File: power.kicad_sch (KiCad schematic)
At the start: 2 parts, among them J301 Conn_01x01_Socket, J302 Conn_01x01_Socket

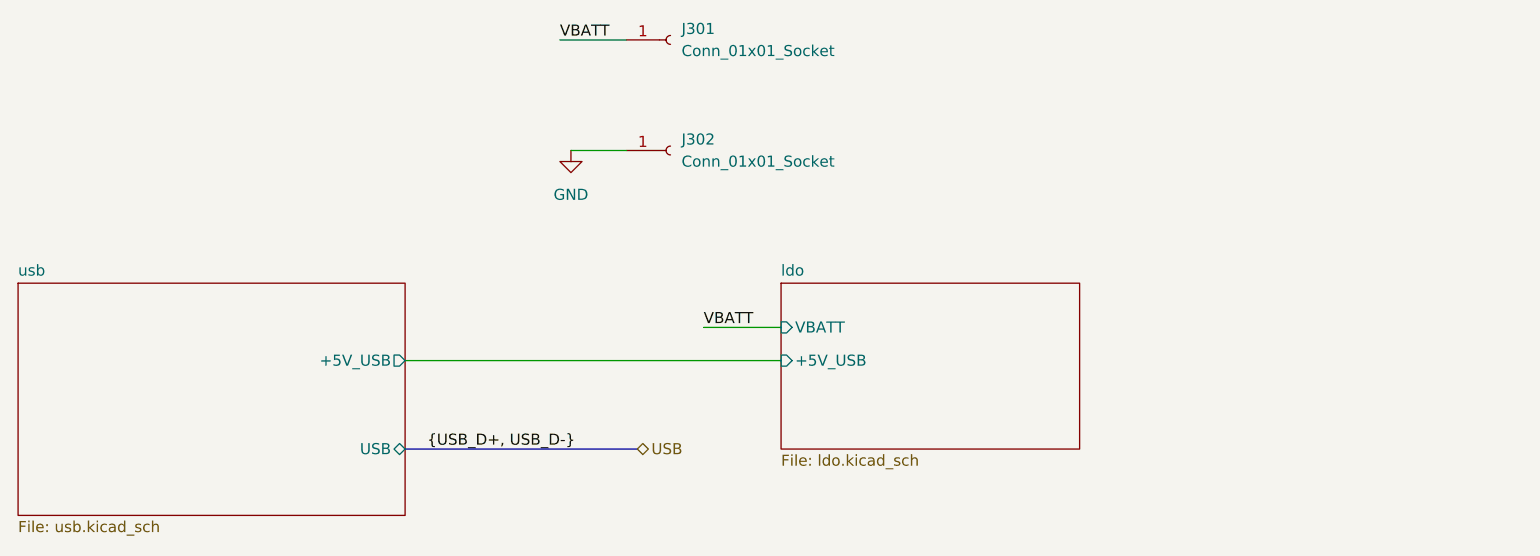
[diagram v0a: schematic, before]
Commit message: added motor controller
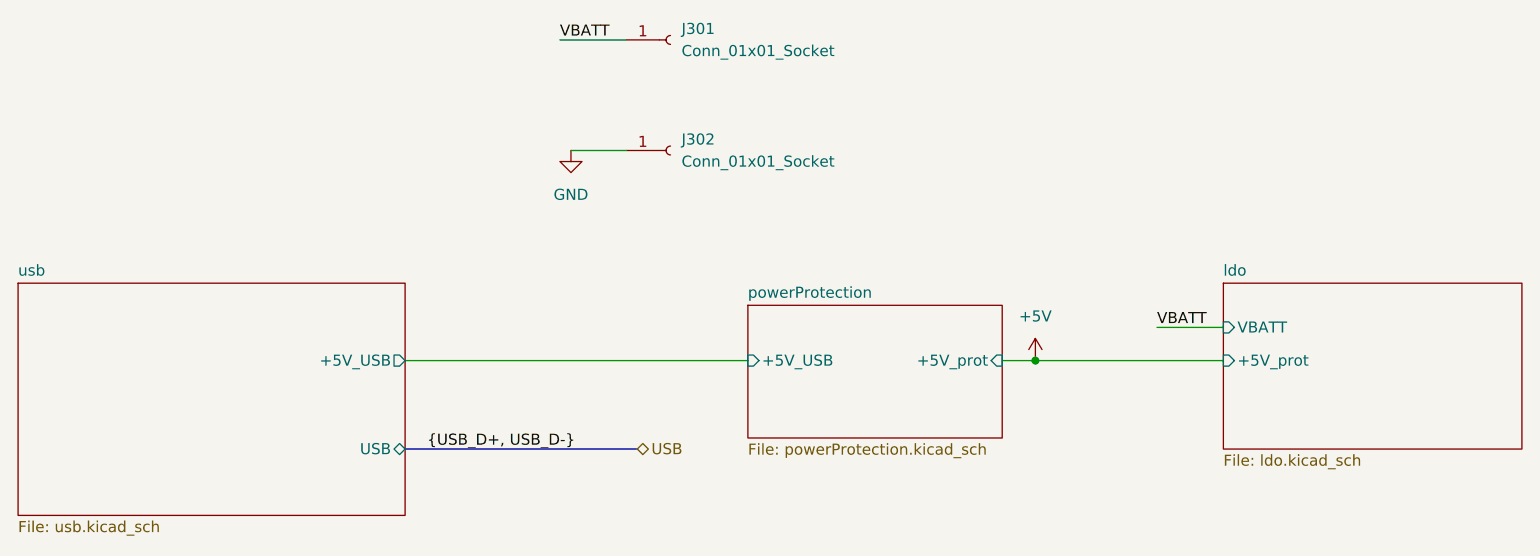
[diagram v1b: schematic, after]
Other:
- added sheet powerProtection (powerProtection.kicad_sch)
- sheet ldo ports: added +5V_prot; removed +5V_USB
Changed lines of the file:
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@@
 	(generator_version "10.0")
 	(paper "A4")
+	(junction
+		(at 176.53 128.27)
+		(diameter 0)
+		(color 0 0 0 0)
+	)
 	(wire
 		(pts
@@
 	(wire
 		(pts
-			(xy 104.14 128.27) (xy 147.32 128.27)
+			(xy 104.14 128.27) (xy 143.51 128.27)
 		)
 		(stroke
@@
 	(wire
 		(pts
+			(xy 172.72 128.27) (xy 176.53 128.27)
+		)
+		(stroke
+			(width 0)
+			(type default)
+		)
+	)
+	(wire
+		(pts
 			(xy 123.19 104.14) (xy 129.54 104.14)
 		)
@@
 	(wire
 		(pts
-			(xy 138.43 124.46) (xy 147.32 124.46)
+			(xy 190.5 124.46) (xy 198.12 124.46)
+		)
+		(stroke
+			(width 0)
+			(type default)
+		)
+	)
+	(wire
+		(pts
+			(xy 176.53 128.27) (xy 198.12 128.27)
 		)
 		(stroke
@@
 	)
 	(label "VBATT"
-		(at 138.43 124.46 0)
+		(at 190.5 124.46 0)
 		(effects
 			(font
@@
 		)
 	)
+	(symbol
+		(lib_id "power:+5V")
+		(at 176.53 128.27 0)
+		(unit 1)
+		(body_style 1)
+		(exclude_from_sim no)
+		(in_bom yes)
+		(on_board yes)
+		(in_pos_files yes)
+		(dnp no)
+		(fields_autoplaced yes)
+		(property "Reference" "#PWR06"
+			(at 176.53 132.08 0)
+			(hide yes)
+			(show_name no)
+			(do_not_autoplace no)
+			(effects
+				(font
+					(size 1.27 1.27)
+				)
+			)
+		)
+		(property "Value" "+5V"
+			(at 176.53 123.19 0)
+			(show_name no)
+			(do_not_autoplace no)
+			(effects
+				(font
+					(size 1.27 1.27)
+				)
+			)
+		)
+		(property "Footprint" ""
+			(at 176.53 128.27 0)
+			(hide yes)
+			(show_name no)
+			(do_not_autoplace no)
+			(effects
+				(font
+					(size 1.27 1.27)
+				)
+			)
+		)
+		(property "Datasheet" ""
+			(at 176.53 128.27 0)
+			(hide yes)
+			(show_name no)
+			(do_not_autoplace no)
+			(effects
+				(font
+					(size 1.27 1.27)
+				)
+			)
+		)
+		(property "Description" "Power symbol creates a global label with name \"+5V\""
+			(at 176.53 128.27 0)
+			(hide yes)
+			(show_name no)
+			(do_not_autoplace no)
+			(effects
+				(font
+					(size 1.27 1.27)
+				)
+			)
+		)
+		(pin "1"
+		)
+		(instances
+			(project "watt_city_car_pcb"
+				(path "/72ee6c6c-9225-4cd9-b8d3-156d5f3d5230/59e3dad0-55dc-4a04-87f2-2c349902244d"
+					(reference "#PWR06")
+					(unit 1)
+				)
+			)
+		)
+	)
 	(sheet
-		(at 147.32 119.38)
+		(at 143.51 121.92)
+		(size 29.21 15.24)
+		(exclude_from_sim no)
+		(in_bom yes)
+		(on_board yes)
+		(dnp no)
+		(fields_autoplaced yes)
+		(stroke
+			(width 0.1524)
+			(type solid)
+		)
+		(fill
+			(color 0 0 0 0)
+		)
+		(property "Sheetname" "powerProtection"
+			(at 143.51 121.2084 0)
+			(show_name no)
+			(do_not_autoplace no)
+			(effects
+				(font
+					(size 1.27 1.27)
+				)
+				(justify left bottom)
+			)
+		)
+		(property "Sheetfile" "powerProtection.kicad_sch"
+			(at 143.51 137.7446 0)
+			(show_name no)
+			(do_not_autoplace no)
+			(effects
+				(font
+					(size 1.27 1.27)
+				)
+				(justify left top)
+			)
+		)
+		(pin "+5V_prot" input
+			(at 172.72 128.27 0)
+			(effects
+				(font
+					(size 1.27 1.27)
+				)
+				(justify right)
+			)
+		)
+		(pin "+5V_USB" input
+			(at 143.51 128.27 180)
+			(effects
+				(font
+					(size 1.27 1.27)
+				)
+				(justify left)
+			)
+		)
+		(instances
+			(project "watt_city_car_pcb"
+				(path "/72ee6c6c-9225-4cd9-b8d3-156d5f3d5230/59e3dad0-55dc-4a04-87f2-2c349902244d"
+					(page "9")
+				)
+			)
+		)
+	)
+	(sheet
+		(at 198.12 119.38)
 		(size 34.29 19.05)
 		(exclude_from_sim no)
@@
 		)
 		(property "Sheetname" "ldo"
-			(at 147.32 118.6684 0)
+			(at 198.12 118.6684 0)
 			(show_name no)
 			(do_not_autoplace no)
@@
 		)
 		(property "Sheetfile" "ldo.kicad_sch"
-			(at 147.32 139.0146 0)
+			(at 198.12 139.0146 0)
 			(show_name no)
 			(do_not_autoplace no)
@@
 		)
 		(property "Field2" ""
-			(at 147.32 119.38 0)
+			(at 198.12 119.38 0)
 			(hide yes)
 			(show_name no)
@@
 		)
 		(pin "VBATT" input
-			(at 147.32 124.46 180)
+			(at 198.12 124.46 180)
 			(effects
 				(font
@@
 			)
 		)
-		(pin "+5V_USB" input
-			(at 147.32 128.27 180)
-			(effects
-				(font
+		(pin "+5V_prot" input
+			(at 198.12 128.27 180)
+			(effects
+				(font
